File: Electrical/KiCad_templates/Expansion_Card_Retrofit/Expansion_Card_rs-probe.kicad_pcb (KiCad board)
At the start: 2 copper layers, 24 x 27.3 mm, 88 parts, among them J10 Conn_01x01, J11 Conn_01x01, J5 tag-connect-swd, P1 USB_C_Plug_USB2.0, Q1 NTZD3155C or CMLDM3757-TR-PBF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, SW1 EVQ-P2002W, U10 74LVC1T45GM,115, U11 74LVC1T45GM,115, U12 NCP133AMXADJTCG, U13 NCP133AMXADJTCG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

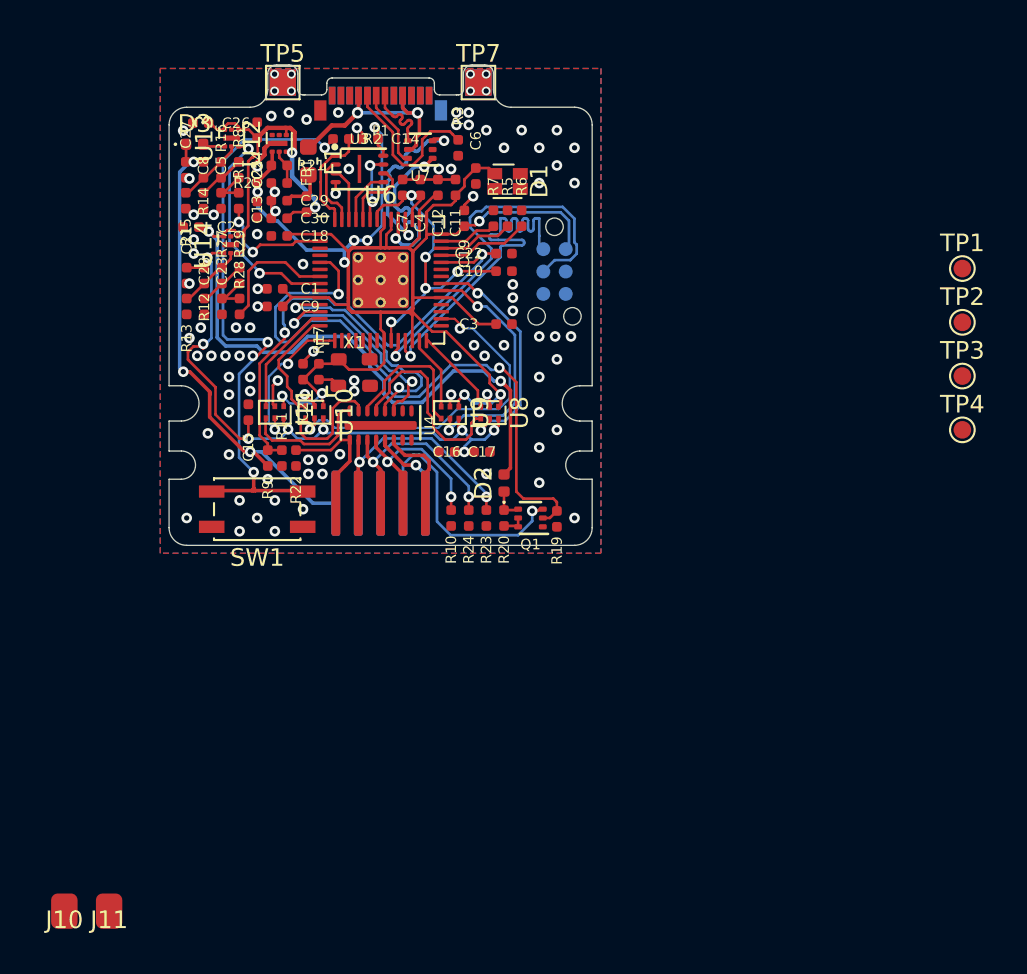
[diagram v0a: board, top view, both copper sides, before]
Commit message: silkscreen and DRC progress
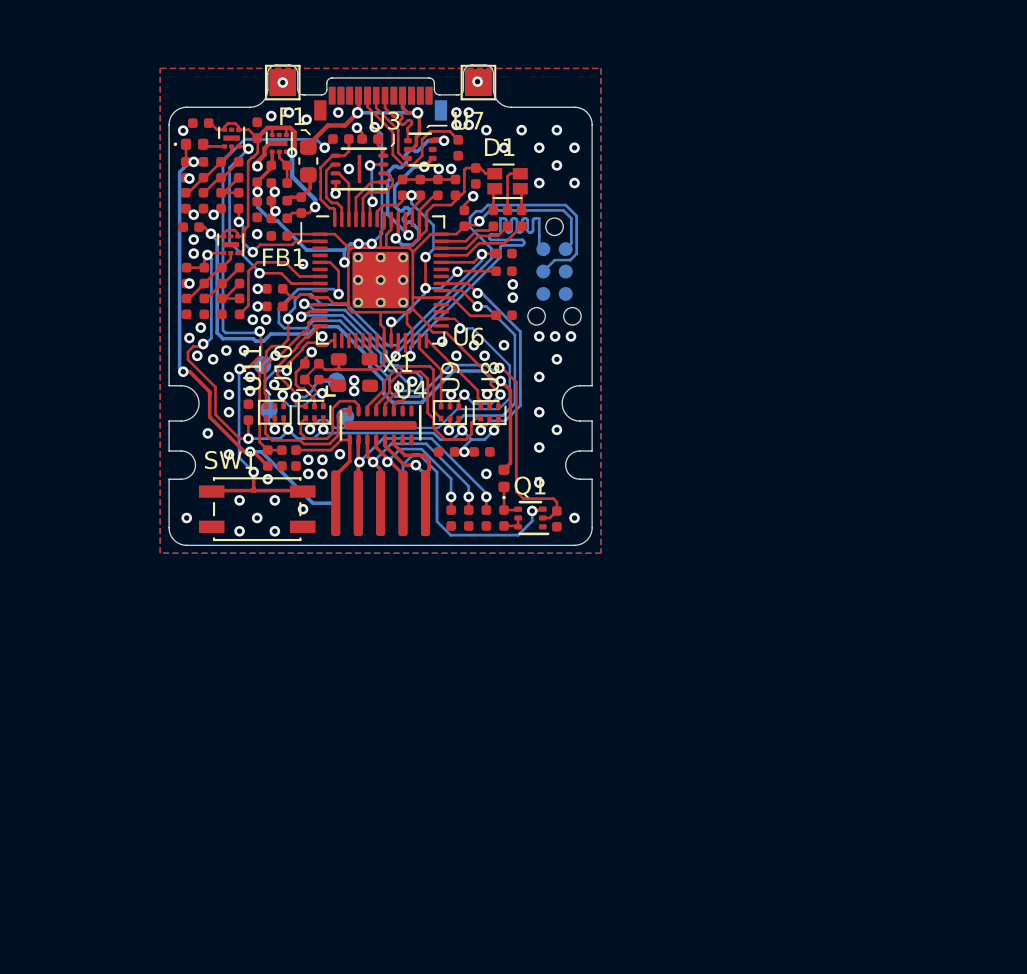
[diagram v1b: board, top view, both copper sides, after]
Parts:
- removed J10, J11: Conn_01x01, connectors:pad_1.5x2.0mm
- TP1, TP2, TP3, TP4: moved to B.Cu
- moved TP1 40.2 mm to (133.7, 146.9), turned to 180 degrees
- moved TP4 39.9 mm to (133.3, 144.3), turned to 180 degrees
- moved TP3 35.5 mm to (137.5, 145.2), turned to 180 degrees
- moved TP2 35.4 mm to (138.0, 147.2), turned to 180 degrees
- moved C3 0.50 mm to (147.0, 141.5)
- moved FB1 0.30 mm to (135.5, 135.2)
- moved D2 0.26 mm to (147.0, 150.8)
- moved C20 0.10 mm to (135.7, 144.7)
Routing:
- net Net-(D1-RK): track 0.00 -> 2.71 mm
- net /SWDCLK_JCLK: track 6.63 -> 9.31 mm, vias 0 -> 1
- net /5V_KEY_EN: track 36.4 -> 35.1 mm
- net +3.3V: track 103.8 -> 105.2 mm
- net Net-(D1-GK): track 0.00 -> 1.26 mm
- net Net-(D1-BK): track 0.00 -> 1.26 mm
- net /SWDIO_TMS: track 6.50 -> 7.72 mm, vias 0 -> 1
- net /~{RESET}: track 12.7 -> 11.6 mm
- net /GNDDetect: track 14.1 -> 13.2 mm
- net /DIR_SWO_TDO: track 14.9 -> 14.2 mm
- net GND: track 16.1 -> 16.8 mm, vias 98 -> 92
- net /DIR_SWDCLK_JCLK: track 20.1 -> 20.8 mm
